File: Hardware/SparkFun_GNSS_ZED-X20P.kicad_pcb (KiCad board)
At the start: 4 copper layers, 43.2 x 43.2 mm, 142 parts, among them J1 USB_C_Receptacle, J10 U.FL, J11 Conn_01x06, J2 Conn_01x06, J3 Conn_01x09, J4 Qwiic_RA, J5 SMA_Edge, J7 Qwiic_RA, J8 JST_Locking_4, J9 I2C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

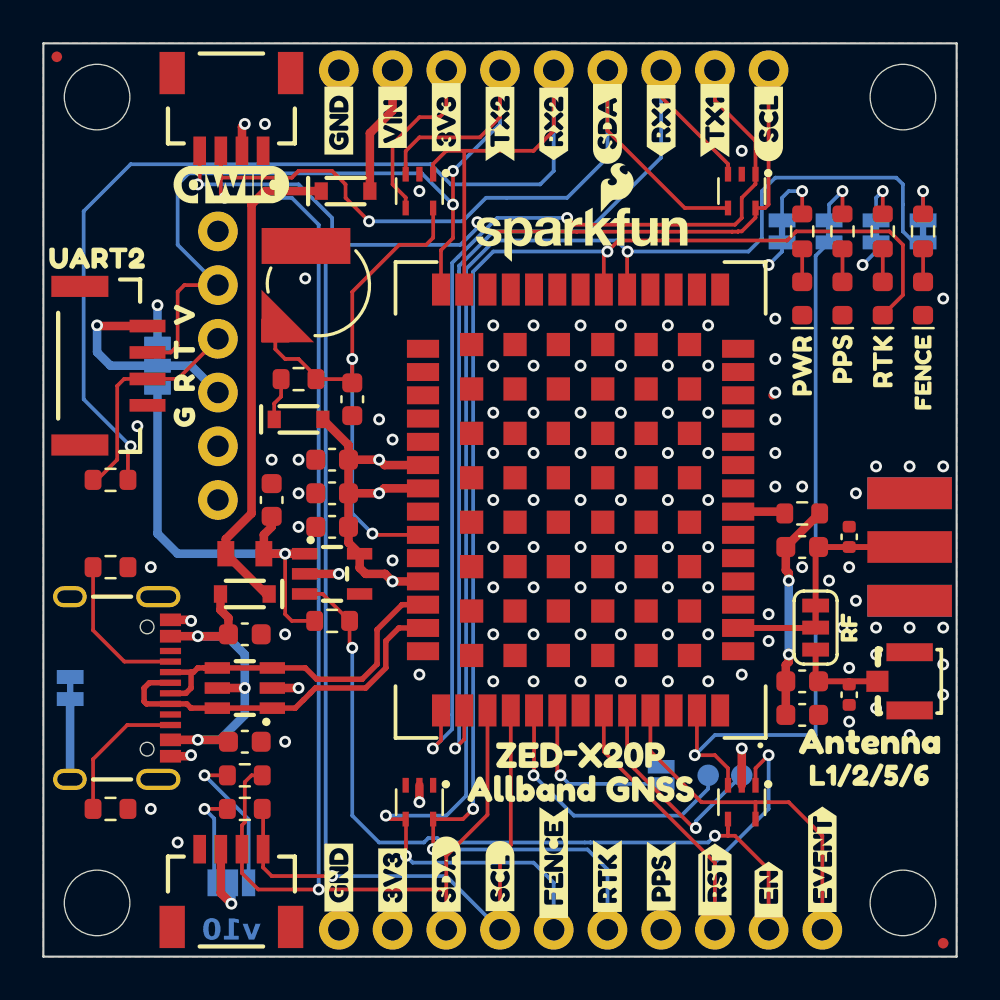
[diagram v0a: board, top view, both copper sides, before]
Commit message: Add CH342
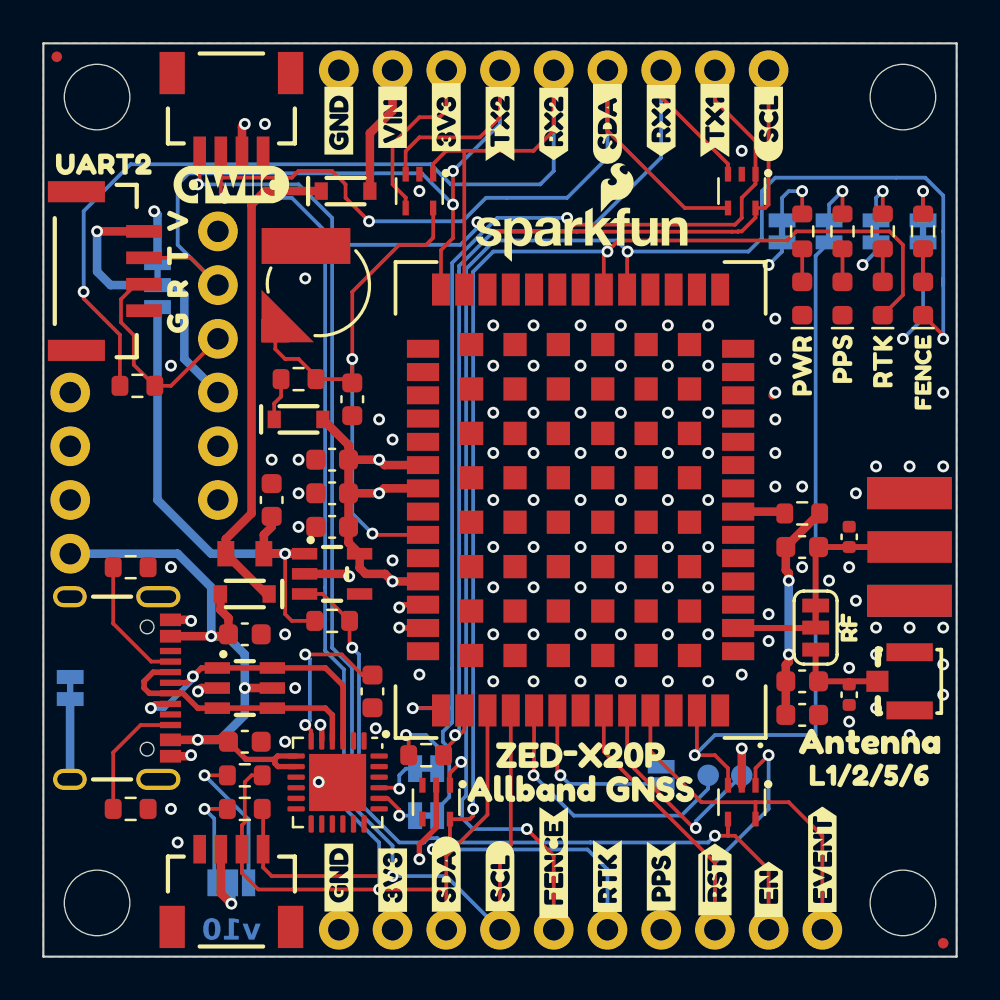
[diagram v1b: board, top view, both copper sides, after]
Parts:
- removed kibuzzard-67EC5C53: G***, kibuzzard-67EC5C53
- added C10: 0.1uF, SparkFun-Capacitor:C_0603_1608Metric, F.Cu at (150.8, 104.9)
- added J6: Conn_01x04, SparkFun-Connector:1x04, F.Cu at (136.5, 98.4)
- added JP11: ~, SparkFun-Jumper:Jumper_2_NC_Trace, B.Cu at (153.4, 108.6)
- added JP12: ~, SparkFun-Jumper:Jumper_2_NC_Trace, B.Cu at (153.4, 110.8)
- added R10: 1k, SparkFun-Resistor:R_0603_1608Metric, F.Cu at (153.4, 108.0)
- added U4: CH342F, SparkFun-Semiconductor-Standard:QFN-24-1EP_4x4mm_P0.5mm_EP2.7x2.7mm, F.Cu at (149.2, 109.2)
- added kibuzzard-66CB830B: G***, kibuzzard-66CB830B, B.Cu at (138.4, 98.4)
- added kibuzzard-67FD7838: G***, kibuzzard-67FD7838, B.Cu at (138.4, 90.8)
- added kibuzzard-67FD783C: G***, kibuzzard-67FD783C, B.Cu at (138.4, 93.3)
- added kibuzzard-67FD7841: G***, kibuzzard-67FD7841, B.Cu at (139.1, 95.9)
- added kibuzzard-67FD789E: G***, kibuzzard-67FD789E, B.Cu at (150.8, 110.8)
- added kibuzzard-67FD78AA: G***, kibuzzard-67FD78AA, B.Cu at (150.8, 108.6)
- added kibuzzard-67FD78C4: G***, kibuzzard-67FD78C4, B.Cu at (164.5, 106.4)
- L1, L2: value 33nH -> 47nH
- moved kibuzzard-66CB82FB 8.89 mm to (140.7, 83.2)
- moved R8 4.62 mm to (139.7, 90.5), turned to 180 degrees
- moved J8 4.48 mm to (138.3, 85.1)
- moved kibuzzard-6797CF40 4.46 mm to (141.6, 85.1)
- moved kibuzzard-67EC5939 4.46 mm to (138.1, 80.0)
- moved JP4 3.81 mm to (140.7, 85.7)
- moved kibuzzard-66CB829C 3.81 mm to (138.7, 85.7)
- moved kibuzzard-66CB830B 1.11 mm to (140.7, 88.3)
- moved R1 0.95 mm to (139.4, 110.5)
- moved R2 0.95 mm to (139.4, 99.1)
- moved D13 0.79 mm to (153.8, 110.2)
- turned U1 to 0 degrees
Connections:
- D13 pad 1: unconnected-(D13-K1-Pad1) -> GEO_STAT
- D13 pad 4: GEO_STAT -> unconnected-(D13-K3-Pad4)
- D9 pad 1: GND -> GEO_STAT
- J1 pad A6: USB_D+ -> Net-(U1-I/O1)
- J1 pad A7: USB_D- -> Net-(U1-I/O2)
- J1 pad B6: USB_D+ -> Net-(U1-I/O1)
- J1 pad B7: USB_D- -> Net-(U1-I/O2)
- JP8 pad 2: GEO_STAT -> 3.3V
- U1 pad 1: USB_D+ -> Net-(U1-I/O1)
- U1 pad 3: USB_D- -> Net-(U1-I/O2)
- U1 pad 4: USB_D- -> Net-(U1-I/O2)
- U1 pad 6: USB_D+ -> Net-(U1-I/O1)
- U5 pad 39: USB_D- -> /D-
- U5 pad 40: USB_D+ -> /D+
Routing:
- net /D-: track 0.00 -> 22.7 mm, vias 0 -> 1
- net /D+: track 0.00 -> 20.2 mm, vias 0 -> 1
- net USB_D+: track 17.6 -> 0.00 mm
- net USB_D-: track 16.5 -> 0.00 mm
- net Net-(U1-I/O1): track 0.00 -> 15.1 mm, vias 0 -> 2
- net VUSB: track 17.1 -> 31.0 mm
- net Net-(U1-I/O2): track 0.00 -> 12.4 mm
- net Net-(U4-V3): track 0.00 -> 7.96 mm, vias 0 -> 2
- net 3.3V: track 36.2 -> 43.1 mm, vias 8 -> 10
- net TX1/POCI: track 48.2 -> 53.0 mm
- net RX2: track 58.5 -> 53.8 mm
- net VOUT: track 9.85 -> 14.0 mm
- net Net-(JP11-B): track 0.00 -> 3.76 mm, vias 0 -> 1
- net GND: track 7.57 -> 10.9 mm, vias 108 -> 111
- net 5V: track 21.6 -> 24.4 mm
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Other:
- board text added: "Material: TG135"
- board text removed: "Material: TG155"
